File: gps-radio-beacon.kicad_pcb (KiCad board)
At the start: 2 copper layers, 106.4 x 69.7 mm, 40 parts, among them J1 Conn_01x16, J2 Conn_01x16, J3 Conn_Coaxial, J4 Conn_Coaxial, J5 Screw_Terminal_01x04, P1 USB_C_Plug_USB2.0, Q1 Q_PMOS_DGS, U1 PGA2040, U2 RFM95W-915S2, U3 MAX-M10S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

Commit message: Revert "bendy traces"
This reverts commit 8a4ff923ad6d744258f9f7e3ddda1145dac49418.
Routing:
- net VCC: track 154.7 -> 156.1 mm
- net +3V3: track 206.2 -> 205.0 mm
- net /GPS_TIMEPULSE: track 48.2 -> 49.4 mm
- net /IND_LED_2: track 46.2 -> 47.2 mm
- net /GPS_SDA: track 57.9 -> 58.8 mm
- net VBUS: track 55.5 -> 56.4 mm
- net /GPS_SCL: track 56.5 -> 57.3 mm
- net /IND_LED_1: track 46.9 -> 47.7 mm
- net /PWR-USB/USB_D+: track 38.8 -> 39.5 mm
- net /PWR-USB/USB_D-: track 36.1 -> 36.8 mm
- net /IND_LED_3: track 39.8 -> 40.4 mm
- net /RADIO_IRQ: track 40.7 -> 41.2 mm
- net /GPS_RESET: track 50.5 -> 51.0 mm

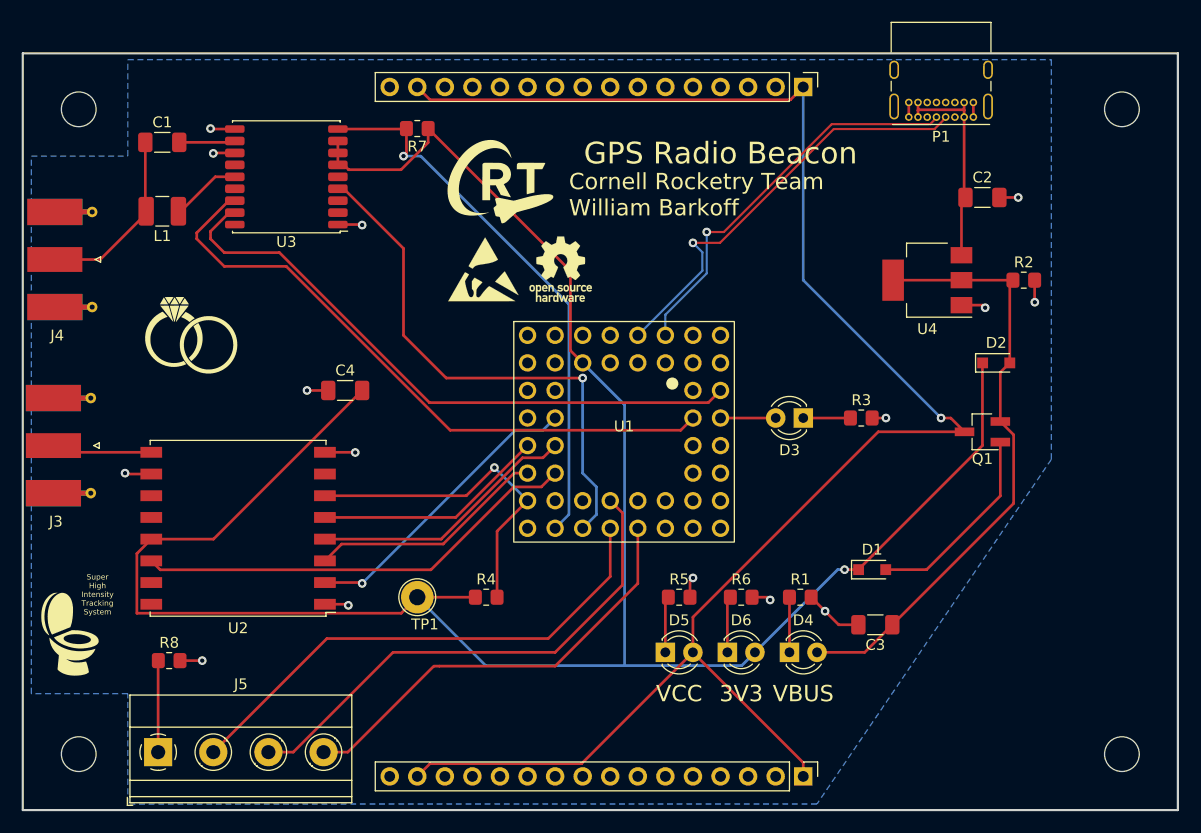
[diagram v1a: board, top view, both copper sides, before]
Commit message: bendy traces
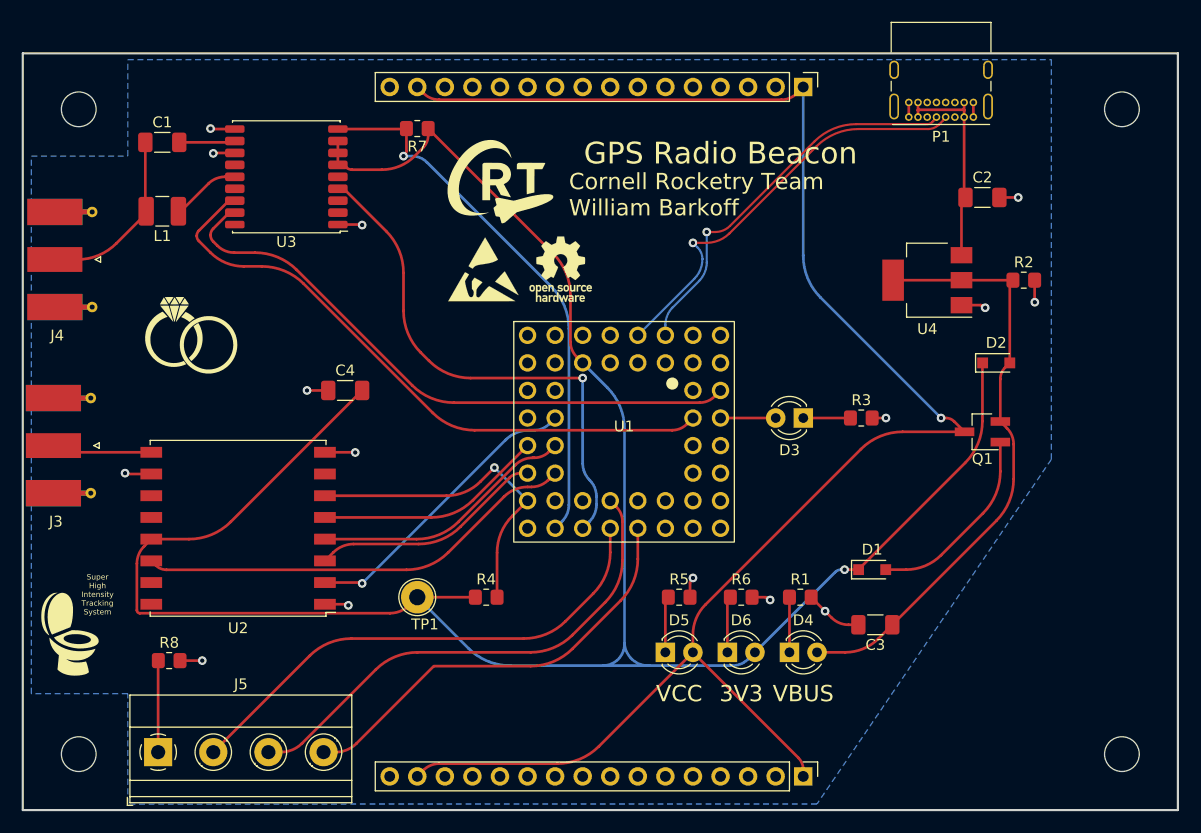
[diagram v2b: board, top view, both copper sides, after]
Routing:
- net VCC: track 156.1 -> 154.7 mm
- net +3V3: track 205.0 -> 206.2 mm
- net /GPS_TIMEPULSE: track 49.4 -> 48.2 mm
- net /IND_LED_2: track 47.2 -> 46.2 mm
- net /GPS_SDA: track 58.8 -> 57.9 mm
- net VBUS: track 56.4 -> 55.5 mm
- net /GPS_SCL: track 57.3 -> 56.5 mm
- net /IND_LED_1: track 47.7 -> 46.9 mm
- net /PWR-USB/USB_D+: track 39.5 -> 38.8 mm
- net /PWR-USB/USB_D-: track 36.8 -> 36.1 mm
- net /IND_LED_3: track 40.4 -> 39.8 mm
- net /RADIO_IRQ: track 41.2 -> 40.7 mm
- net /GPS_RESET: track 51.0 -> 50.5 mm
